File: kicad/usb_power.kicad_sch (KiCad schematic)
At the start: 39 parts, among them J1 USB_C_Receptacle_USB2.0_14P, J3 Conn_01x02, Q1 IRLML6402, SW25 SW_Push_DPDT, U12 CH340N, U13 TP4056-42-ESOP8, U14 SX1308, U15 LM393

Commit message: HW: Fix SX1308 footprint TSOT23-5 -> TSOT23-6
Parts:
- U14: footprint Package_TO_SOT_SMD:TSOT-23-5 -> Package_TO_SOT_SMD:TSOT-23-6
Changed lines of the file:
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@@
 			)
 		)
-		(property "Footprint" "Package_TO_SOT_SMD:TSOT-23-5"
+		(property "Footprint" "Package_TO_SOT_SMD:TSOT-23-6"
 			(at 101.6 127 0)
 			(effects

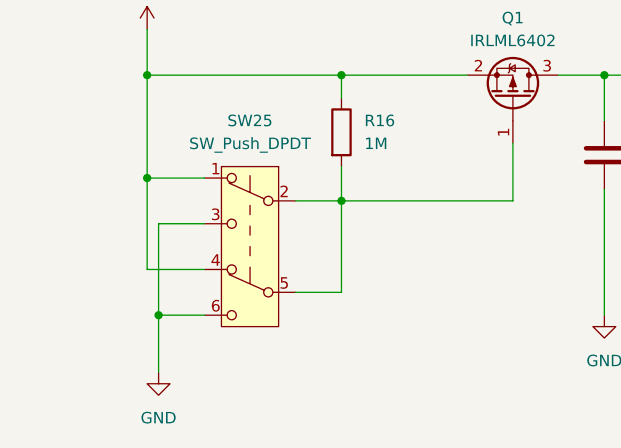
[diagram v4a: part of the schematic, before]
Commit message: HW: Fix power switch pinout
thx kicad for no coherent pin numeration convention
and random shuffle on footprint assigment...
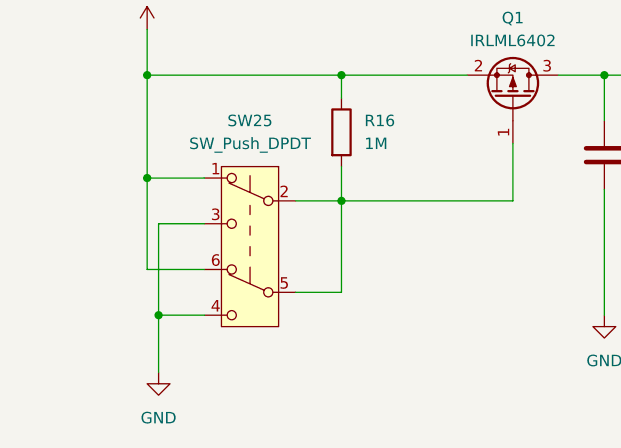
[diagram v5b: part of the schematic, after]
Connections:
- net +BATT: now also SW25.6 (A); no longer SW25.4 (A)
- net GND: now also SW25.4 (C); no longer SW25.6 (C)
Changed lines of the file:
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@@
 	(title_block
 		(title "USB and power management")
-		(date "2025-12-04")
-		(rev "B")
+		(date "2025-12-17")
+		(rev "C")
 		(company "A.K.")
 	)
